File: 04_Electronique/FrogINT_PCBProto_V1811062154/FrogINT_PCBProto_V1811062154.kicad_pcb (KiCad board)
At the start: 2 copper layers, 41.6 x 53.7 mm, 32 parts, among them J1 USB_B_Mini, J2 Conn_01x01_Female, J3 Conn_01x03, J4 JTAG, Q1 PMV48XP, Q2 PMV48XP, U1 NCP1117-5.0_SOT223, U2 LP2985-3.3, U3 ATmega16U4RC-AU, Y1 16MHz

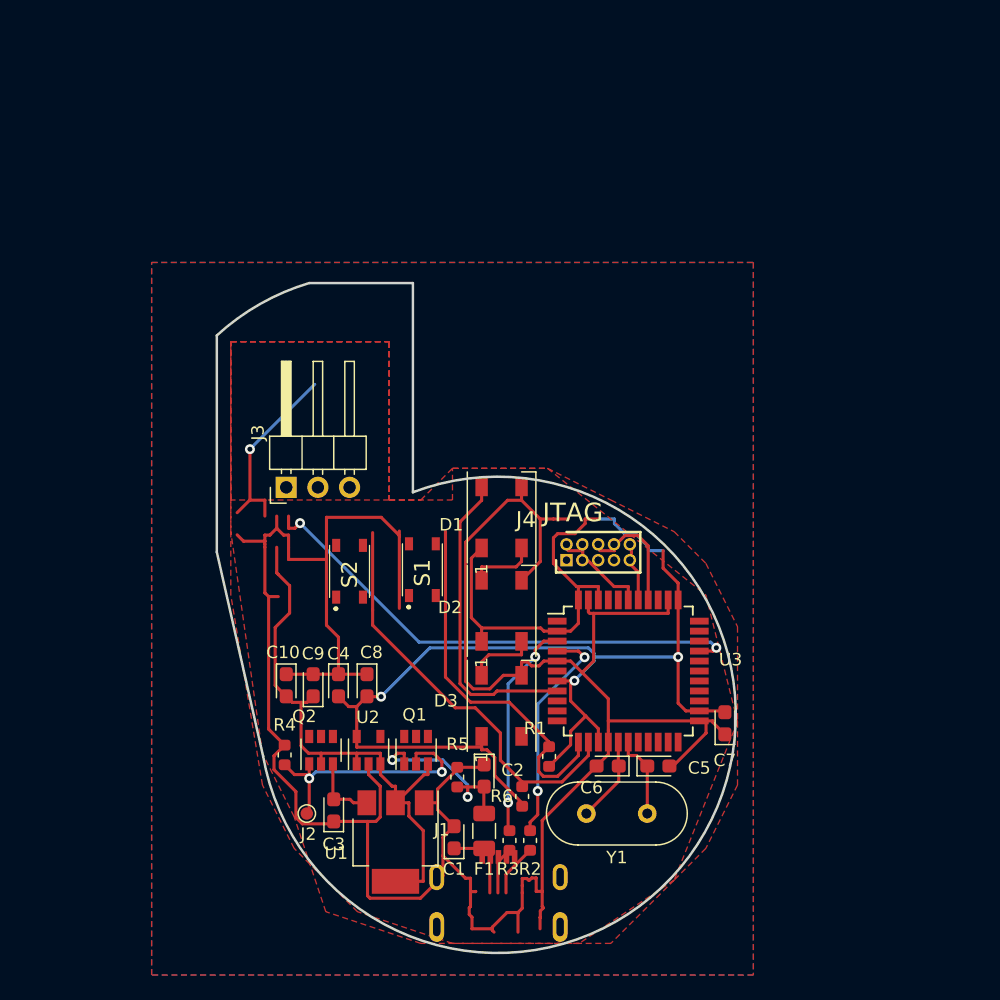
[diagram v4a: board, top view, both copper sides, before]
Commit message: Commit du 26/03/2019 :
 - Refonte du PCB --> passage en circulaire de 3,8mm de diamètre
 - Mise à jour des librairies avec notamment création de la librairie atmega16u4-au
 - Mise à jour de la librairie sur le connecteur USB pour ajouter les CTRL.YBCK -> limite du composant
 - Suppression de la fonction d'alimention 3V3 au profit d'une seule alimentation en 5V. Attention, il faut cependant corriger le naming
 - Changement du connecteur pour le TouchSensor (femelle)
 - ajout d'un R/C + pad pour souder directement une antenne pour tester le Sensor Capacitif
 - suppression du bouton reset et du bouton interrupt.
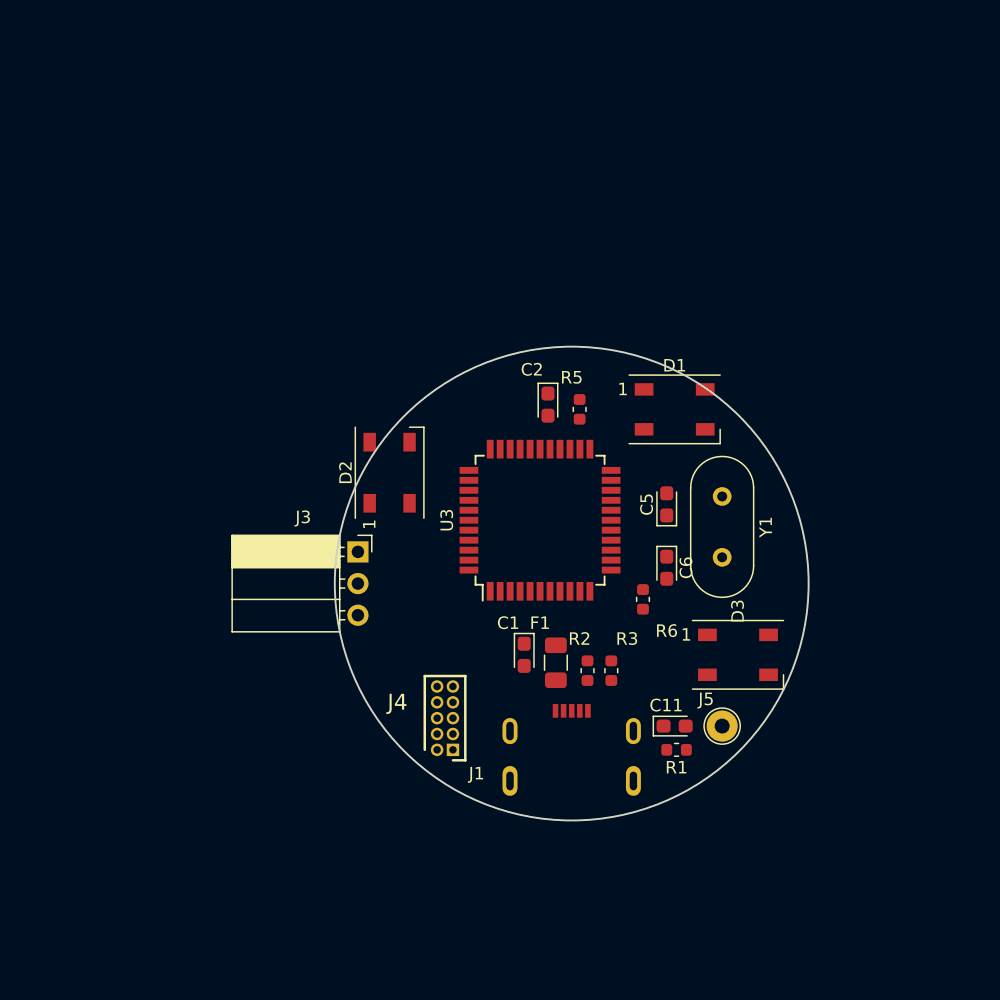
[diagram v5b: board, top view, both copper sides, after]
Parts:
- removed C10, C3: 100nF, FTA_FrogINT_Library_Footprint_Package:CP_EIA-2012-12_Kemet-R
- removed C4, C7: 0.1µF, FTA_FrogINT_Library_Footprint_Package:CP_EIA-2012-12_Kemet-R
- removed C8: 1µF, FTA_FrogINT_Library_Footprint_Package:CP_EIA-2012-12_Kemet-R
- removed C9: 22µF, FTA_FrogINT_Library_Footprint_Package:CP_EIA-2012-12_Kemet-R
- removed J2: Conn_01x01_Female, TestPoint:TestPoint_Pad_D1.0mm
- removed Q1, Q2: PMV48XP, Package_TO_SOT_SMD:SOT-23-6
- removed R4: 10k, FTA_FrogINT_Library_Footprint_Package:R_0603_1608Metric
- removed S1, S2: PTS810SJG250SMTRLFS, SamacSys_Parts:PTS810SJG250SMTRLFS
- removed U1: NCP1117-5.0_SOT223, Package_TO_SOT_SMD:SOT-223-3_TabPin2
- removed U2: LP2985-3.3, Package_TO_SOT_SMD:SOT-23-5
- added C11: 22pF, FTA_FrogINT_Library_Footprint_Package:CP_EIA-2012-12_Kemet-R, F.Cu at (156.8, 116.4)
- added J5: Conn_01x01_Female, TestPoint:TestPoint_THTPad_D2.5mm_Drill1.2mm, F.Cu at (160.6, 116.4)
- J3: footprint Connector_PinHeader_2.54mm:PinHeader_1x03_P2.54mm_Horizontal -> Connector_PinSocket_2.54mm:PinSocket_1x03_P2.54mm_Horizontal
- U3: value ATmega16U4RC-AU -> ATmega16U4-AU; footprint FTA_FrogINT_Library_Footprint_Package:TQFP-44_10x10mm_P0.8mm -> Package_QFP:TQFP-44_10x10mm_P0.8mm
- moved R5 31.1 mm to (149.1, 91.0)
- moved C2 30.2 mm to (146.6, 90.6)
- moved Y1 26.1 mm to (160.6, 98.0), turned to 270 degrees
- moved C5 21.0 mm to (156.1, 98.7), turned to 90 degrees
- moved D3 19.4 mm to (161.8, 110.7), turned to 0 degrees
- moved R6 18.5 mm to (154.2, 106.3)
- moved J4 17.7 mm to (139.0, 118.3), turned to 90 degrees
- moved C6 16.6 mm to (156.1, 103.7), turned to 270 degrees
- moved D1 16.4 mm to (156.8, 91.0), turned to 0 degrees
- moved R3 15.9 mm to (151.7, 112.0)
- moved C1 15.7 mm to (144.7, 110.7), turned to 270 degrees
- moved F1 14.7 mm to (147.2, 111.3), turned to 90 degrees
- moved R2 14.4 mm to (149.8, 112.0)
- moved D2 14.3 mm to (133.9, 96.1)
- moved U3 14.0 mm to (146.0, 99.9), turned to 90 degrees
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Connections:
- C2 pad 2: VBUS -> +3V3
- D3 pad 2: Net-(D3-Pad2) -> (no net)
- F1 pad 1: VBUS -> +3V3
- J1 pad 4: Net-(J1-Pad4) -> (no net)
- R1 pad 1: +3V3 -> /Input_Interrupt
- R1 pad 2: /Input_Interrupt -> GND
- R5 pad 1: VBUS -> +3V3
- U3 pad 1: Net-(U3-Pad1) -> (no net)
- U3 pad 10: Net-(U3-Pad10) -> (no net)
- U3 pad 11: Net-(U3-Pad11) -> (no net)
- U3 pad 18: Net-(U3-Pad18) -> (no net)
- U3 pad 19: Net-(U3-Pad19) -> (no net)
- U3 pad 20: Net-(U3-Pad20) -> (no net)
- U3 pad 21: Net-(U3-Pad21) -> (no net)
- U3 pad 22: Net-(U3-Pad22) -> (no net)
- U3 pad 25: Net-(U3-Pad25) -> (no net)
- U3 pad 26: Net-(U3-Pad26) -> (no net)
- U3 pad 27: Net-(U3-Pad27) -> (no net)
- U3 pad 28: Net-(U3-Pad28) -> (no net)
- U3 pad 29: Net-(U3-Pad29) -> (no net)
- U3 pad 31: Net-(U3-Pad31) -> (no net)
- U3 pad 32: Net-(U3-Pad32) -> (no net)
- U3 pad 33: Net-(U3-Pad33) -> (no net)
- U3 pad 40: Net-(U3-Pad40) -> (no net)
- U3 pad 41: Net-(U3-Pad41) -> (no net)
- U3 pad 6: Net-(U3-Pad6) -> (no net)
- U3 pad 9: Net-(U3-Pad9) -> (no net)
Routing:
- net GND: track 224.4 -> 0.00 mm
- net +3V3: track 113.6 -> 0.00 mm, vias 3 -> 0
- net +5V: track 46.5 -> 0.00 mm
- net /Input_Int_Touch: track 41.1 -> 0.00 mm, vias 2 -> 0
- net /reset: track 33.5 -> 0.00 mm
- net /Input_Interrupt: track 30.0 -> 0.00 mm
- net Net-(D1-Pad4): track 24.8 -> 0.00 mm
- net /Vin: track 21.2 -> 0.00 mm, vias 2 -> 0
- net /D+: track 18.1 -> 0.00 mm, vias 2 -> 0
- net /D-: track 17.5 -> 0.00 mm, vias 2 -> 0
- net /Cap-TouchSensor: track 15.4 -> 0.00 mm, vias 1 -> 0
- net VBUS: track 15.1 -> 0.00 mm, vias 2 -> 0
- net Net-(J3-Pad3): track 9.29 -> 0.00 mm
- net Net-(J3-Pad1): track 7.31 -> 0.00 mm
- net Net-(C6-Pad1): track 6.82 -> 0.00 mm
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- removed copper zone on B.Cu, net GND
- removed copper zone on F.Cu, net GND
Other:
- board size 41.6 x 53.7 mm -> 38 x 38 mm
- board text removed: "JTAG"

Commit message: Evolution de la V3 :
 + Creation d'un modèle pour les LED WS2812 avec HeatSink (Footprint + meca3D)
 + Creation d'un modèle pour Fusible (Footprint + Meca3D)

Autre évolution majeure :
•	Ligne USB – Faire une paire différentielle
•	Supprimer le switch « normal » pour ne conserver que le switch « reset ».
o	OK
•	Mais router en externe une GPIO
o	OK mutualisé avec R/C pour Touche sensor
•	Suppression du TouchPad au profit d’un connecteur 2.54 coudé – femelle. ATTENTION actuellement de type mâle à remplacer à femelle.
o	OK
o	Genre du header à remplacer de mâle à femelle
•	Ajouter R & C pour tester le TouchPanel avec une feuille d’alu.
o	OK mutualisé avec R/C pour Touche sensor
•	Créer une Pin externe avec de connecter la feuille d’alu.
o	OK mutualisé avec R/C pour Touche sensor
•	Supprimer la génération du 5V non nécessaire
o	Laisser en l’état
•	Supprimer la pin de mesure de 5V
o	Laisser en l’état
•	Remplacement connecteur JTAG au pas de 2.54 par un au pas de 1,27 qui doit rester compatible avec interface ATMEL-Ice.
o	OK en cours.
o	Pinout à vérifier.
•	Remplacement du Quartz par un modèle 3.2x2.4
o	OK
•	Mise à jour du modèle 3D du fusible
o	OK
•	routage dont ligne différentielle.
o	OK
•	Passer à diamètre supérieur le PCB
o	OK
•	Remplacer le package des LED
o	OK
•	Mise à jour de la BOM RadioSpare
o	OK
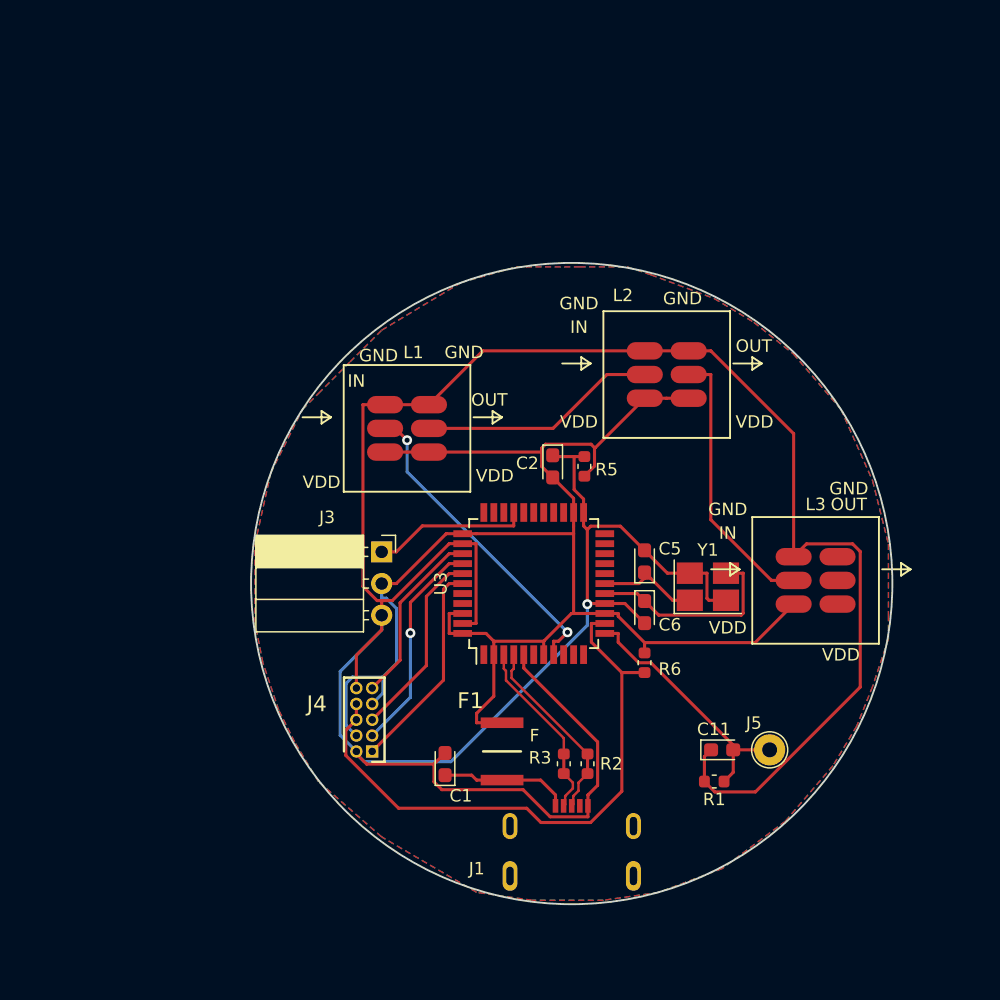
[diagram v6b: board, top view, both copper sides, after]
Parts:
- removed D1, D2, D3: WS2812B, FTA_FrogINT_Library_Footprint_Package:LED_WS2812B_PLCC4_5.0x5.0mm_P3.2mm
- added G***: LOGO, FTA_FrogINT_Library_Footprint_Package:Logo_Thales_Silk_Bottom, F.Cu at (148.5, 119.0)
- added G***: LOGO, FTA_FrogINT_Library_Footprint_Package:Logo_CCSL_Silk_Bottom, F.Cu at (148.5, 87.9)
- added L1: LED, FTA_FrogINT_Library_Footprint_Package:WS2812-LED_HeatSink, F.Cu at (135.3, 92.6)
- added L2: LED, FTA_FrogINT_Library_Footprint_Package:WS2812-LED_HeatSink, F.Cu at (156.1, 88.2)
- added L3: LED, FTA_FrogINT_Library_Footprint_Package:WS2812-LED_HeatSink, F.Cu at (168.1, 104.7)
- F1: footprint Fuse:Fuse_1206_3216Metric -> FTA_FrogINT_Library_Footprint_Package:FUSC4632X85N
- Y1: value 16MHz -> XTal TSX-3225 16MHz; footprint FTA_FrogINT_Library_Footprint_Package:Crystal_HC49-U_Vertical -> Crystal:Crystal_SMD_SeikoEpson_TSX3225-4Pin_3.2x2.5mm_HandSoldering
- moved C1 10.8 mm to (138.3, 119.5), turned to 90 degrees
- moved R3 8.38 mm to (147.9, 119.5)
- moved F1 8.32 mm to (142.9, 118.5), turned to 270 degrees
- moved J1 7.62 mm to (148.5, 130.4)
- moved R2 7.47 mm to (149.8, 119.5)
- moved Y1 7.33 mm to (159.4, 105.3), turned to 0 degrees
- moved J4 6.48 mm to (132.5, 118.5)
- moved U3 5.11 mm to (145.5, 105.0)
- moved R6 5.08 mm to (154.3, 111.3), turned to 270 degrees
- moved C2 4.97 mm to (147.0, 95.6)
- moved C5 4.91 mm to (154.3, 103.2)
- moved R5 4.59 mm to (149.5, 95.6)
- moved C11 4.26 mm to (160.6, 118.3)
- moved J5 4.26 mm to (164.4, 118.3)
- moved C6 3.98 mm to (154.3, 107.3)
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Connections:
- J1 pad 2: Net-(J1-Pad2) -> /D-
- J1 pad 3: Net-(J1-Pad3) -> /D+
- R2 pad 2: Net-(J1-Pad3) -> /D+
- R3 pad 2: Net-(J1-Pad2) -> /D-
- Y1 pad 2: Net-(C6-Pad1) -> GND
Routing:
- net GND: track 0.00 -> 238.0 mm, vias 0 -> 1
- net +3V3: track 0.00 -> 124.0 mm
- net /reset: track 0.00 -> 47.3 mm
- net Net-(L1-Pad2): track 0.00 -> 25.4 mm, vias 0 -> 2
- net Net-(L2-Pad5): track 0.00 -> 22.1 mm
- net /Input_Interrupt: track 0.00 -> 20.6 mm
- net Net-(L1-Pad5): track 0.00 -> 19.1 mm
- net Net-(J4-Pad3): track 0.00 -> 17.4 mm, vias 0 -> 1
- net Net-(J4-Pad1): track 0.00 -> 17.1 mm
- net Net-(C6-Pad1): track 0.00 -> 16.5 mm
- net Net-(J4-Pad5): track 0.00 -> 15.4 mm
- net /D+: track 0.00 -> 15.3 mm
- net /D-: track 0.00 -> 14.7 mm
- net Net-(J4-Pad9): track 0.00 -> 14.4 mm
- net /Input_Int_Touch: track 0.00 -> 12.5 mm
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- added copper zone on B.Cu, net GND
- added copper zone on F.Cu, net GND
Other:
- board size 38 x 38 mm -> 51.4 x 51.4 mm
